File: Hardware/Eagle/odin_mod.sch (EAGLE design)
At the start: 36 parts

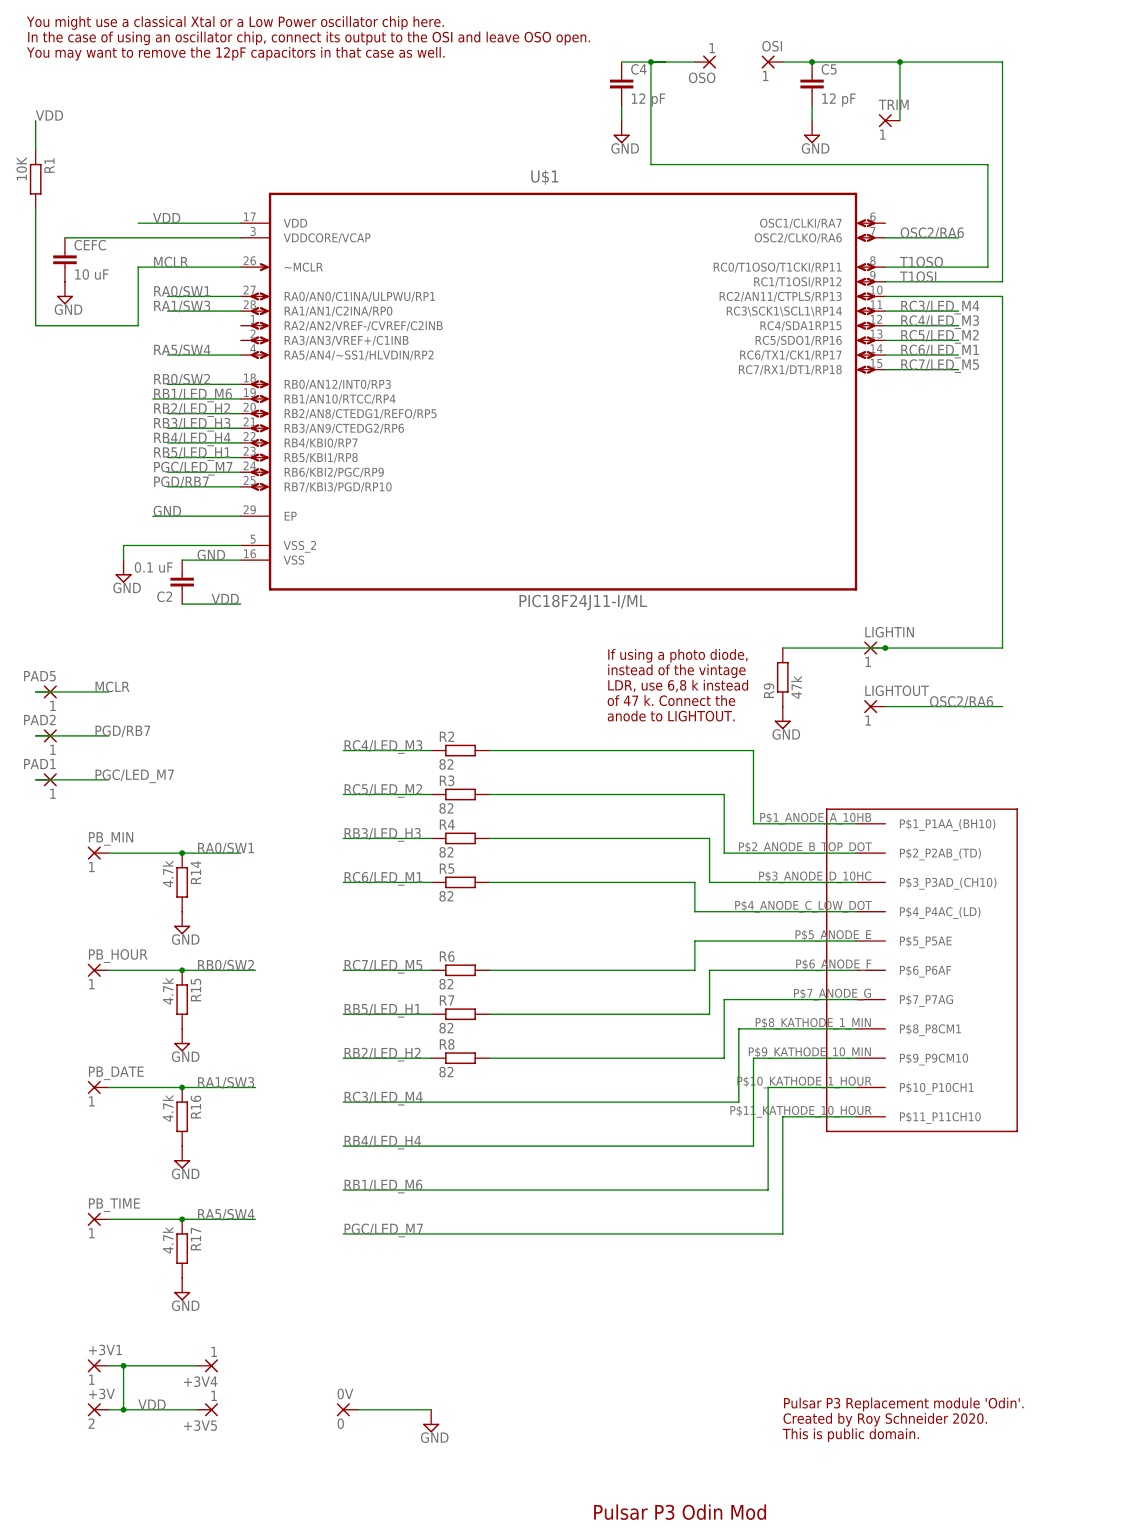
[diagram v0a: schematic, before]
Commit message: Optimized Odin and Loki layout.
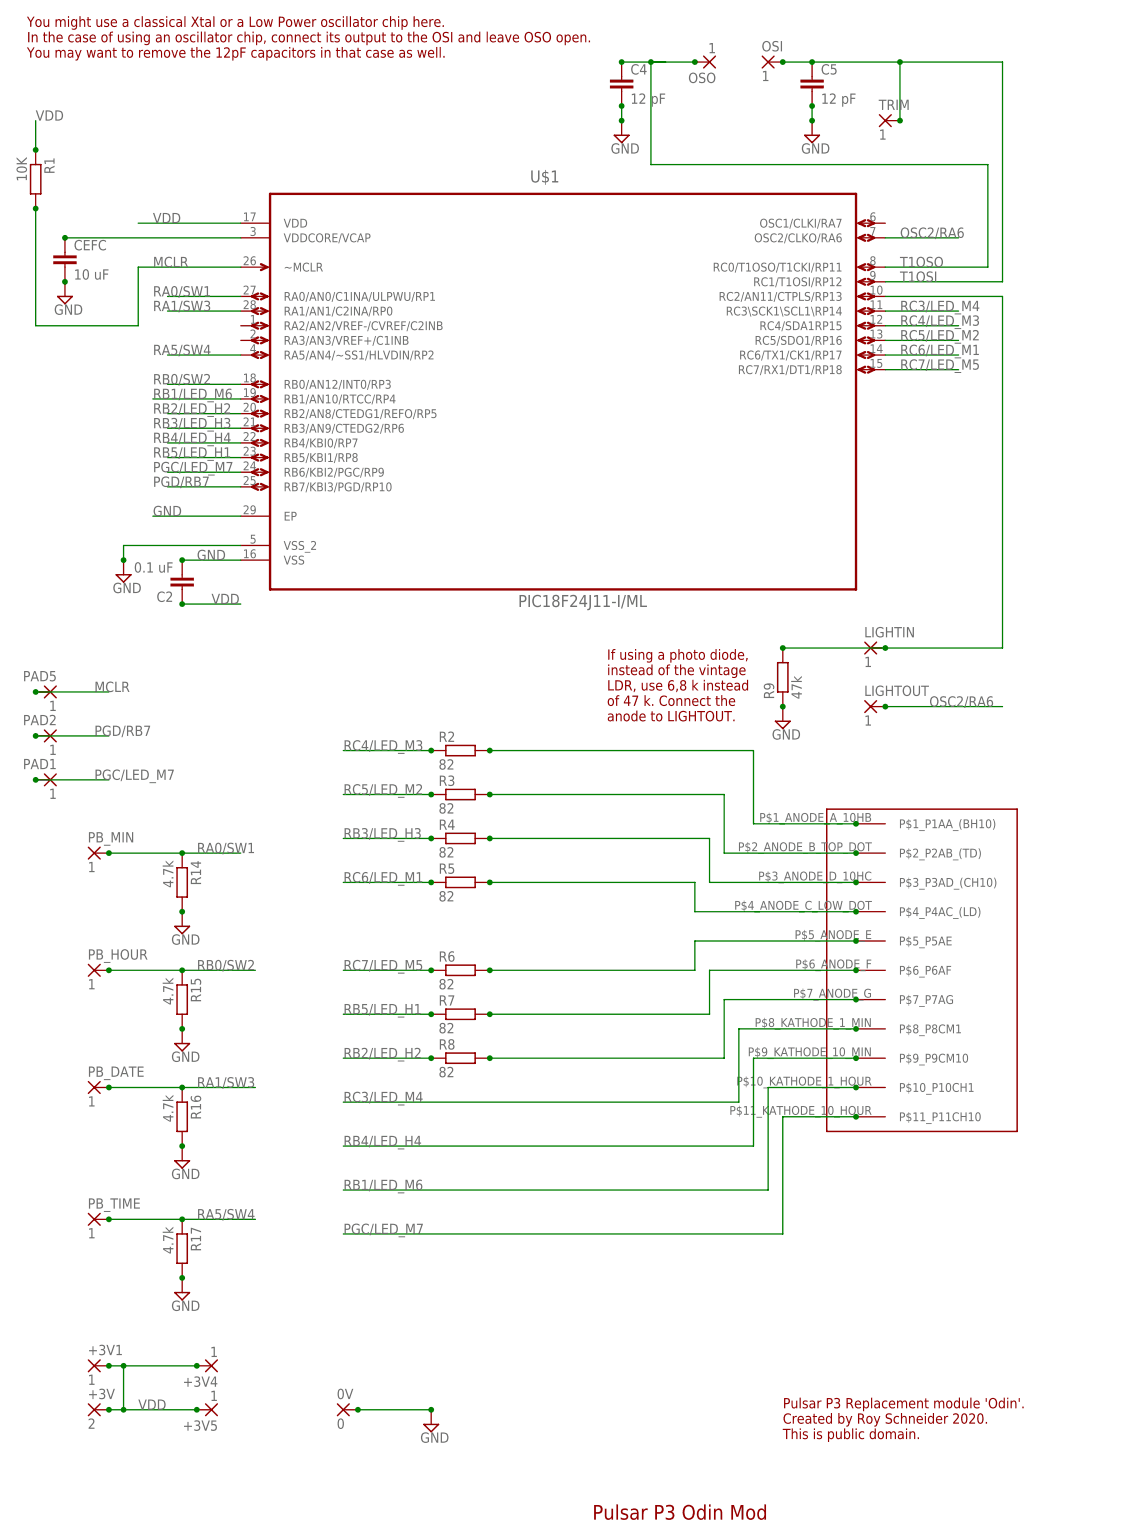
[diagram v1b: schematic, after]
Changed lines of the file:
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@@
 <wire x1="-83.82" y1="58.42" x2="-104.14" y2="58.42" width="0.1524" layer="91"/>
 <wire x1="-104.14" y1="58.42" x2="-104.14" y2="55.88" width="0.1524" layer="91"/>
+<junction x="-104.14" y="55.88"/>
 </segment>
 <segment>
 <pinref part="CEFC" gate="G$1" pin="2"/>
 <pinref part="SUPPLY2" gate="GND" pin="GND"/>
+<junction x="-114.3" y="104.14"/>
 </segment>
 <segment>
@@
 <wire x1="-83.82" y1="55.88" x2="-93.98" y2="55.88" width="0.1524" layer="91"/>
 <label x="-91.44" y="55.88" size="1.778" layer="95"/>
+<junction x="-93.98" y="55.88"/>
 </segment>
 <segment>
@@
 <wire x1="-63.5" y1="-91.44" x2="-50.8" y2="-91.44" width="0.1524" layer="91"/>
 <pinref part="0V" gate="1" pin="P"/>
+<junction x="-63.5" y="-91.44"/>
+<junction x="-50.8" y="-91.44"/>
 </segment>
 <segment>
@@
 <pinref part="SUPPLY7" gate="GND" pin="GND"/>
 <wire x1="-17.78" y1="134.62" x2="-17.78" y2="132.08" width="0.1524" layer="91"/>
+<junction x="-17.78" y="134.62"/>
+<junction x="-17.78" y="132.08"/>
 </segment>
 <segment>
@@
 <pinref part="SUPPLY8" gate="GND" pin="GND"/>
 <wire x1="15.24" y1="134.62" x2="15.24" y2="132.08" width="0.1524" layer="91"/>
+<junction x="15.24" y="132.08"/>
+<junction x="15.24" y="134.62"/>
 </segment>
 <segment>
 <pinref part="R14" gate="G$1" pin="2"/>
 <pinref part="SUPPLY1" gate="GND" pin="GND"/>
+<junction x="-93.98" y="-5.08"/>
 </segment>
 <segment>
 <pinref part="R15" gate="G$1" pin="2"/>
 <pinref part="SUPPLY5" gate="GND" pin="GND"/>
+<junction x="-93.98" y="-25.4"/>
 </segment>
 <segment>
 <pinref part="SUPPLY9" gate="GND" pin="GND"/>
 <pinref part="R16" gate="G$1" pin="2"/>
+<junction x="-93.98" y="-45.72"/>
 </segment>
 <segment>
 <pinref part="SUPPLY10" gate="GND" pin="GND"/>
 <pinref part="R17" gate="G$1" pin="2"/>
+<junction x="-93.98" y="-68.58"/>
 </segment>
 <segment>
 <pinref part="R9" gate="G$1" pin="1"/>
 <pinref part="SUPPLY4" gate="GND" pin="GND"/>
+<junction x="10.16" y="30.48"/>
 </segment>
 </net>
@@
 <pinref part="R1" gate="G$1" pin="2"/>
 <wire x1="-119.38" y1="96.52" x2="-119.38" y2="116.84" width="0.1524" layer="91"/>
+<junction x="-119.38" y="116.84"/>
 </segment>
 <segment>
@@
 <label x="-109.22" y="33.02" size="1.778" layer="95"/>
 <pinref part="PAD5" gate="1" pin="P"/>
+<junction x="-119.38" y="33.02"/>
 </segment>
 </net>
@@
 <wire x1="5.08" y1="10.16" x2="5.08" y2="22.86" width="0.1524" layer="91"/>
 <wire x1="5.08" y1="22.86" x2="-40.64" y2="22.86" width="0.1524" layer="91"/>
+<junction x="-40.64" y="22.86"/>
+<junction x="22.86" y="10.16"/>
 </segment>
 </net>
@@
 <wire x1="0" y1="5.08" x2="0" y2="15.24" width="0.1524" layer="91"/>
 <wire x1="0" y1="15.24" x2="-40.64" y2="15.24" width="0.1524" layer="91"/>
+<junction x="-40.64" y="15.24"/>
+<junction x="22.86" y="5.08"/>
 </segment>
 </net>
@@
 <wire x1="-2.54" y1="0" x2="-2.54" y2="7.62" width="0.1524" layer="91"/>
 <wire x1="-2.54" y1="7.62" x2="-40.64" y2="7.62" width="0.1524" layer="91"/>
+<junction x="-40.64" y="7.62"/>
+<junction x="22.86" y="0"/>
 </segment>
 </net>
@@
 <wire x1="-5.08" y1="-5.08" x2="-5.08" y2="0" width="0.1524" layer="91"/>
 <wire x1="-5.08" y1="0" x2="-40.64" y2="0" width="0.1524" layer="91"/>
+<junction x="-40.64" y="0"/>
+<junction x="22.86" y="-5.08"/>
 </segment>
 </net>
@@
 <wire x1="-5.08" y1="-10.16" x2="-5.08" y2="-15.24" width="0.1524" layer="91"/>
 <wire x1="-5.08" y1="-15.24" x2="-40.64" y2="-15.24" width="0.1524" layer="91"/>
+<junction x="-40.64" y="-15.24"/>
+<junction x="22.86" y="-10.16"/>
 </segment>
 </net>
@@
 <wire x1="-2.54" y1="-15.24" x2="-2.54" y2="-22.86" width="0.1524" layer="91"/>
 <wire x1="-2.54" y1="-22.86" x2="-40.64" y2="-22.86" width="0.1524" layer="91"/>
+<junction x="-40.64" y="-22.86"/>
+<junction x="22.86" y="-15.24"/>
 </segment>
 </net>
@@
 <wire x1="0" y1="-20.32" x2="0" y2="-30.48" width="0.1524" layer="91"/>
 <wire x1="0" y1="-30.48" x2="-40.64" y2="-30.48" width="0.1524" layer="91"/>
+<junction x="-40.64" y="-30.48"/>
+<junction x="22.86" y="-20.32"/>
 </segment>
 </net>
@@
 <wire x1="-106.68" y1="5.08" x2="-93.98" y2="5.08" width="0.1524" layer="91"/>
 <junction x="-93.98" y="5.08"/>
+<junction x="-106.68" y="5.08"/>
 </segment>
 <segment>
@@
 <wire x1="-106.68" y1="-15.24" x2="-93.98" y2="-15.24" width="0.1524" layer="91"/>
 <junction x="-93.98" y="-15.24"/>
+<junction x="-106.68" y="-15.24"/>
 </segment>
 <segment>
@@
 <junction x="-104.14" y="-91.44"/>
 <junction x="-104.14" y="-83.82"/>
+<junction x="-106.68" y="-91.44"/>
+<junction x="-106.68" y="-83.82"/>
+<junction x="-91.44" y="-83.82"/>
+<junction x="-91.44" y="-91.44"/>
 </segment>
 <segment>
@@
 <wire x1="-119.38" y1="127" x2="-119.38" y2="132.08" width="0.1524" layer="91"/>
 <label x="-119.38" y="132.08" size="1.778" layer="95"/>
+<junction x="-119.38" y="127"/>
 </segment>
 <segment>
@@
 <wire x1="-93.98" y1="48.26" x2="-83.82" y2="48.26" width="0.1524" layer="91"/>
 <label x="-88.9" y="48.26" size="1.778" layer="95"/>
+<junction x="-93.98" y="48.26"/>
 </segment>
 </net>
@@
 <wire x1="-50.8" y1="-30.48" x2="-66.04" y2="-30.48" width="0.1524" layer="91"/>
 <label x="-66.04" y="-30.48" size="1.778" layer="95"/>
+<junction x="-50.8" y="-30.48"/>
 </segment>
 </net>
@@
 <wire x1="-50.8" y1="7.62" x2="-66.04" y2="7.62" width="0.1524" layer="91"/>
 <label x="-66.04" y="7.62" size="1.778" layer="95"/>
+<junction x="-50.8" y="7.62"/>
 </segment>
 </net>
@@
 <wire x1="5.08" y1="-45.72" x2="-66.04" y2="-45.72" width="0.1524" layer="91"/>
 <label x="-66.04" y="-45.72" size="1.778" layer="95"/>
+<junction x="22.86" y="-30.48"/>
 </segment>
 </net>
@@
 <wire x1="2.54" y1="-25.4" x2="2.54" y2="-38.1" width="0.1524" layer="91"/>
 <wire x1="2.54" y1="-38.1" x2="-66.04" y2="-38.1" width="0.1524" layer="91"/>
+<junction x="22.86" y="-25.4"/>
 </segment>
 </net>
@@
 <wire x1="-50.8" y1="22.86" x2="-66.04" y2="22.86" width="0.1524" layer="91"/>
 <label x="-66.04" y="22.86" size="1.778" layer="95"/>
+<junction x="-50.8" y="22.86"/>
 </segment>
 </net>
@@
 <wire x1="-50.8" y1="15.24" x2="-66.04" y2="15.24" width="0.1524" layer="91"/>
 <label x="-66.04" y="15.24" size="1.778" layer="95"/>
+<junction x="-50.8" y="15.24"/>
 </segment>
 </net>
@@
 <wire x1="-50.8" y1="0" x2="-66.04" y2="0" width="0.1524" layer="91"/>
 <label x="-66.04" y="0" size="1.778" layer="95"/>
+<junction x="-50.8" y="0"/>
 </segment>
 </net>
@@
 <wire x1="-50.8" y1="-15.24" x2="-66.04" y2="-15.24" width="0.1524" layer="91"/>
 <label x="-66.04" y="-15.24" size="1.778" layer="95"/>
+<junction x="-50.8" y="-15.24"/>
 </segment>
 </net>
@@
 <wire x1="-50.8" y1="-22.86" x2="-66.04" y2="-22.86" width="0.1524" layer="91"/>
 <label x="-66.04" y="-22.86" size="1.778" layer="95"/>
+<junction x="-50.8" y="-22.86"/>
 </segment>
 </net>
@@
 <wire x1="10.16" y1="-40.64" x2="10.16" y2="-60.96" width="0.1524" layer="91"/>
 <wire x1="10.16" y1="-60.96" x2="-66.04" y2="-60.96" width="0.1524" layer="91"/>
+<junction x="22.86" y="-40.64"/>
 </segment>
 <segment>
@@
 <label x="-109.22" y="17.78" size="1.778" layer="95"/>
 <pinref part="PAD1" gate="1" pin="P"/>
+<junction x="-119.38" y="17.78"/>
 </segment>
 </net>
@@
 <label x="-109.22" y="25.4" size="1.778" layer="95"/>
 <pinref part="PAD2" gate="1" pin="P"/>
+<junction x="-119.38" y="25.4"/>
 </segment>
 </net>
@@
 <pinref part="OSO" gate="1" pin="P"/>
 <wire x1="-12.7" y1="142.24" x2="-5.08" y2="142.24" width="0.1524" layer="91"/>
+<junction x="-17.78" y="142.24"/>
+<junction x="-5.08" y="142.24"/>
 </segment>
 </net>
@@
 <wire x1="30.48" y1="132.08" x2="30.48" y2="142.24" width="0.1524" layer="91"/>
 <junction x="30.48" y="142.24"/>
+<junction x="10.16" y="142.24"/>
+<junction x="30.48" y="132.08"/>
 </segment>
 </net>
@@
 <wire x1="7.62" y1="-35.56" x2="7.62" y2="-53.34" width="0.1524" layer="91"/>
 <wire x1="7.62" y1="-53.34" x2="-66.04" y2="-53.34" width="0.1524" layer="91"/>
+<junction x="22.86" y="-35.56"/>
 </segment>
 </net>
@@
 <wire x1="-93.98" y1="-35.56" x2="-81.28" y2="-35.56" width="0.1524" layer="91"/>
 <label x="-91.44" y="-35.56" size="1.778" layer="95"/>
+<junction x="-106.68" y="-35.56"/>
 </segment>
 </net>
@@
 <pinref part="CEFC" gate="G$1" pin="1"/>
 <wire x1="-83.82" y1="111.76" x2="-114.3" y2="111.76" width="0.1524" layer="91"/>
+<junction x="-114.3" y="111.76"/>
 </segment>
 </net>
@@
 <wire x1="10.16" y1="40.64" x2="27.94" y2="40.64" width="0.1524" layer="91"/>
 <junction x="27.94" y="40.64"/>
+<junction x="10.16" y="40.64"/>
 </segment>
 </net>
@@
 <wire x1="27.94" y1="30.48" x2="48.26" y2="30.48" width="0.1524" layer="91"/>
 <label x="35.56" y="30.48" size="1.778" layer="95"/>
+<junction x="27.94" y="30.48"/>
 </segment>
 </net>
@@
 <junction x="-93.98" y="-58.42"/>
 <label x="-91.44" y="-58.42" size="1.778" layer="95"/>
-</segment>
-</net>
+<junction x="-106.68" y="-58.42"/>
+</segment>
+</net>

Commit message: Reviewed boards and code.
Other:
- note added: "Do not use less than 10µF here!"
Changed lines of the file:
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@@
 of 47 k. Connect the
 anode to LIGHTOUT.</text>
+<text x="-120.904" y="87.122" size="1.778" layer="94">Do not use
+less than
+10µF here!</text>
 </plain>
 <instances>

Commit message: Optimizations.
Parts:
- R9: value 47k -> 68k
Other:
- note added: "If using a photo diode, instead of the vintage LDR, use 6,8 k instead of 68 k. Connect the anode to LIGHTOUT."
- note removed: "If using a photo diode, instead of the vintage LDR, use 6,8 k instead of 47 k. Connect the anode to LIGHTOUT."
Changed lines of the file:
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@@
 <part name="LIGHTOUT" library="wirepad" deviceset="SMD2" device="" value="1"/>
 <part name="TRIM" library="wirepad" deviceset="SMD2" device="" value="1"/>
-<part name="R9" library="resistor" deviceset="R-EU_" device="R0402" value="47k"/>
+<part name="R9" library="resistor" deviceset="R-EU_" device="R0402" value="68k"/>
 <part name="SUPPLY4" library="supply2" deviceset="GND" device=""/>
 </parts>
@@
 instead of the vintage
 LDR, use 6,8 k instead
-of 47 k. Connect the
+of 68 k. Connect the
 anode to LIGHTOUT.</text>
 <text x="-120.904" y="87.122" size="1.778" layer="94">Do not use

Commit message: Released ODIN MkII featuring n-mos transistors for the common cathodes.
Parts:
- added Q1, Q2, Q3, Q4: IRLML0030, irlml0030:IRLML0030
- added R10, R11, R12, R13: 47k, resistor:R-EU_R0402
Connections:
- new net N$11: Q4.D, U$3.P$11_P11CH10
- new net N$12: Q3.D, U$3.P$10_P10CH1
- new net N$13: Q2.D, U$3.P$9_P9CM10
- new net N$14: Q1.D, U$3.P$8_P8CM1
- net GND: now also Q1.S, Q2.S, Q3.S, Q4.S, R10.2, R11.2, R12.2, R13.2
- net PGC/LED_M7: now also Q4.G, R10.1; no longer U$3.P$11_P11CH10
- net RB1/LED_M6: now also Q3.G, R11.1; no longer U$3.P$10_P10CH1
- net RB4/LED_H4: now also Q2.G, R12.1; no longer U$3.P$9_P9CM10
- net RC3/LED_M4: now also Q1.G, R13.1; no longer U$3.P$8_P8CM1
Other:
- note added: "Pulsar P3 Odin Mk II"
- note added: "Pulsar P3 Replacement module 'Odin Mark II'. Created by Roy Schneider 2023. This is public domain."
- note removed: "Pulsar P3 Odin Mod"
- note removed: "Pulsar P3 Replacement module 'Odin'. Created by Roy Schneider 2020. This is public domain."
- moved on the sheet: 0V

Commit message: Updated image files.
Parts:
- R9: value 68k -> 47k
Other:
- note added: "If using a photo diode, instead of the vintage LDR, use 6,8 k instead of 47 k. Connect the anode to LIGHTOUT. Actually some LDR give you different output. So you might change the resistor value down to 10 k."
- note removed: "If using a photo diode, instead of the vintage LDR, use 6,8 k instead of 68 k. Connect the anode to LIGHTOUT."
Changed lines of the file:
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@@
 <part name="LIGHTOUT" library="wirepad" deviceset="SMD2" device="" value="1"/>
 <part name="TRIM" library="wirepad" deviceset="SMD2" device="" value="1"/>
-<part name="R9" library="resistor" deviceset="R-EU_" device="R0402" value="68k"/>
+<part name="R9" library="resistor" deviceset="R-EU_" device="R0402" value="47k"/>
 <part name="SUPPLY4" library="supply2" deviceset="GND" device=""/>
 <part name="Q1" library="irlml0030" deviceset="IRLML0030" device=""/>
@@
 This is public domain.</text>
 <text x="-22.86" y="-110.49" size="2.54" layer="94" font="vector">Pulsar P3 Odin Mk II</text>
-<text x="-20.32" y="27.94" size="1.778" layer="94">If using a photo diode,
-instead of the vintage
-LDR, use 6,8 k instead
-of 68 k. Connect the
-anode to LIGHTOUT.</text>
+<text x="-45.72" y="27.94" size="1.778" layer="94">If using a photo diode, instead of the vintage
+LDR, use 6,8 k instead of 47 k. Connect the
+anode to LIGHTOUT. Actually some LDR give
+you different output. So you might change
+the resistor value down to 10 k.</text>
 <text x="-120.904" y="87.122" size="1.778" layer="94">Do not use
 less than
